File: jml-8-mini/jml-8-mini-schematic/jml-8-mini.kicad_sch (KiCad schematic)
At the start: 7 parts, among them J1 Barrel_Jack, SW1 SW_DPDT_x2, U1 Z80CPU, U2 28HC64, U3 60L256, U4 Z80 CTC, U6 Z80 SIO

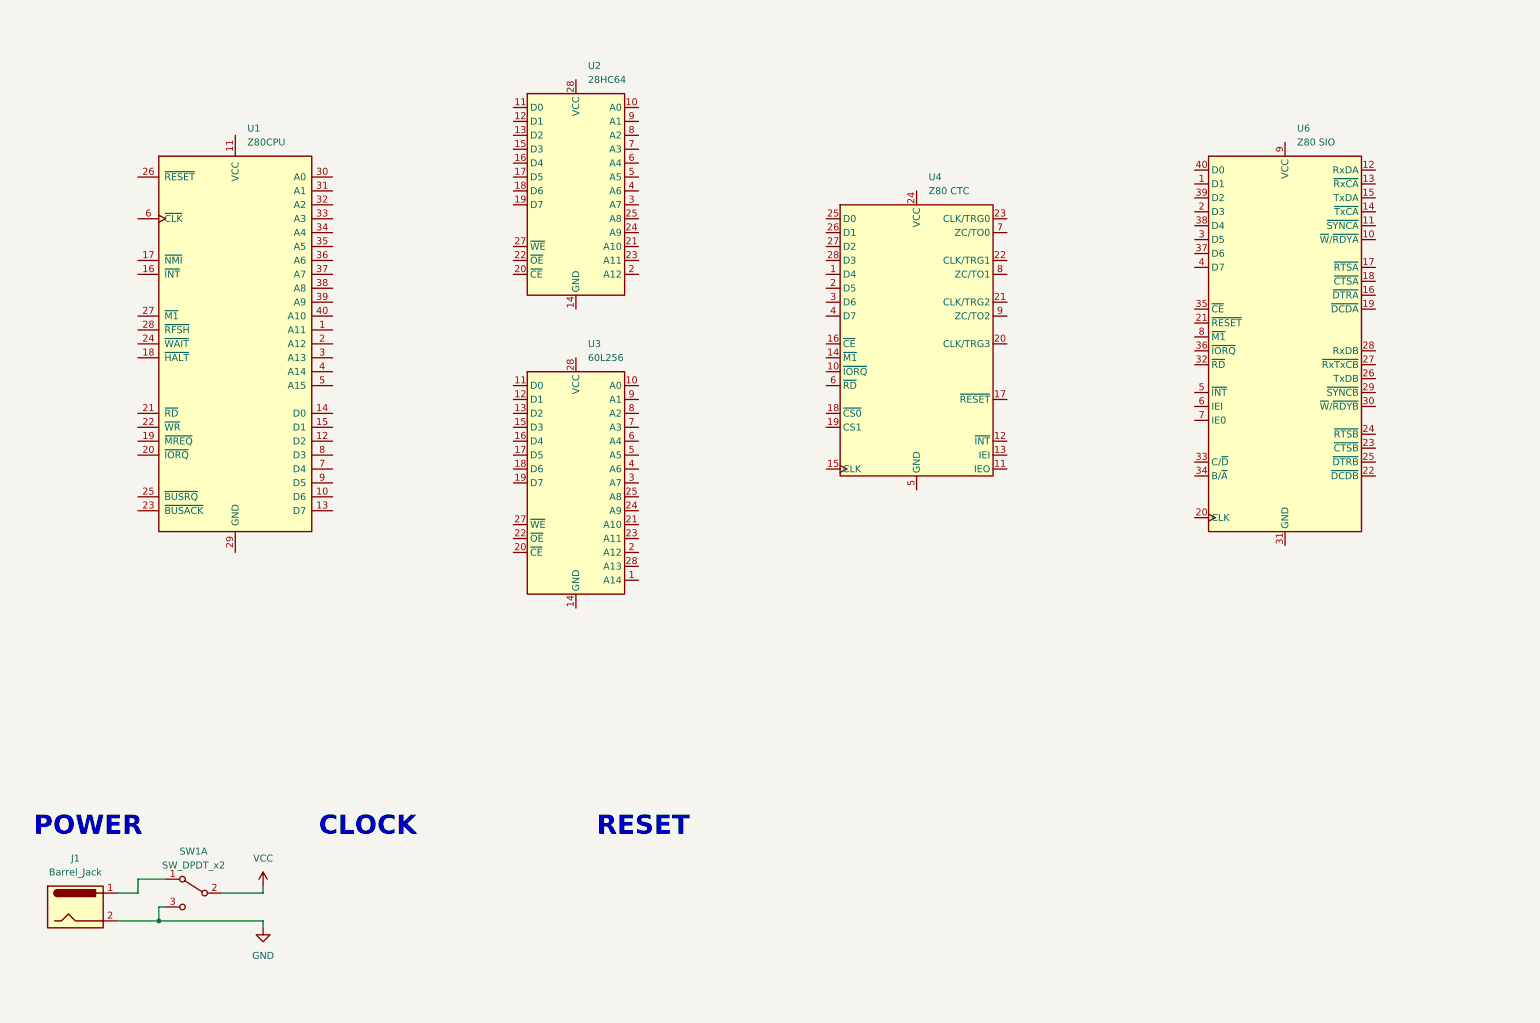
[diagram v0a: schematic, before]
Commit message: updates to jml-8 mini schematic
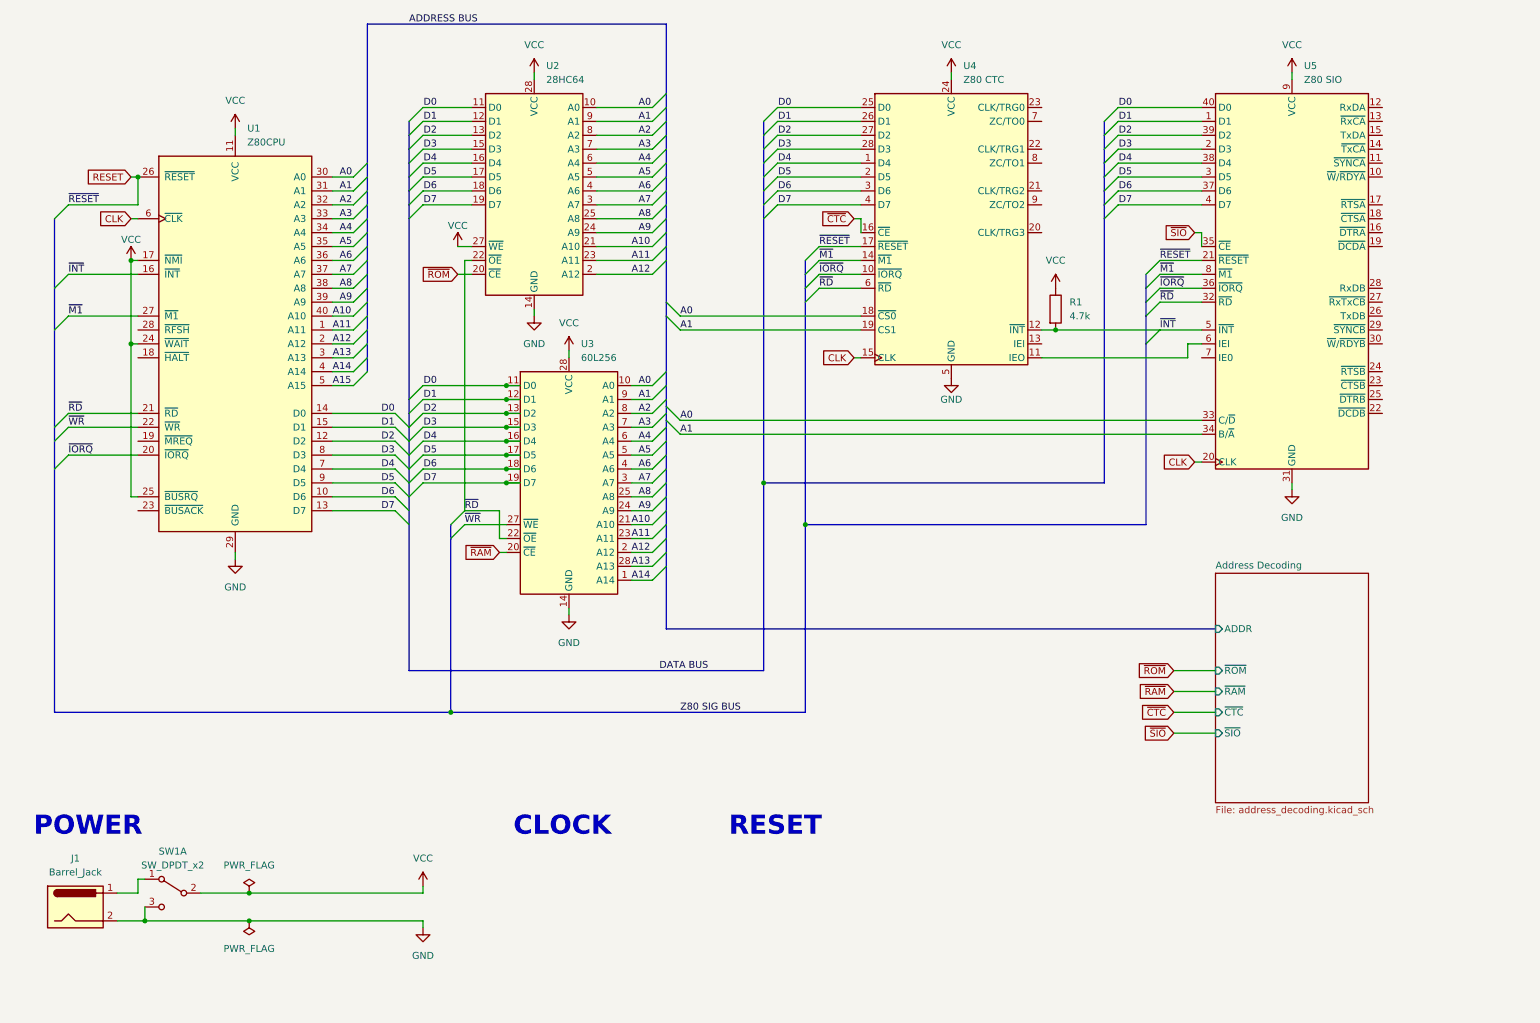
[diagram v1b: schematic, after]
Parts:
- removed U6: Z80 SIO, Package_DIP:DIP-40_W15.24mm_LongPads, symbol jml-8-mini-library:Z80_SIO/0
- added R1: 4.7k, symbol Device:R
- added U5: Z80 SIO, symbol jml-8-mini-library:Z80_SIO/0
- U4: footprint Package_DIP:DIP-28_W15.24mm_LongPads -> (none)
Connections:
- net GND: now also U1.29 (GND), U2.14 (GND), U3.14 (GND), U4.5 (GND), U5.31 (GND)
- net VCC: now also U1.11 (VCC), U1.17 (~{NMI}), U1.24 (~{WAIT}), U1.25 (~{BUSRQ}), U2.27 (~{WE}), U2.28 (VCC), U3.28 (VCC), U4.24 (VCC), R1.1, U5.9 (VCC)
- net A0: now reaches U2.10 (A0)
- net A0: now also U1.30 (A0), U3.10 (A0), U4.18 (~{CS0}), U5.33 (C/~{D})
- net D0: now reaches U2.11 (D0)
- net D0: now also U1.14 (D0), U3.11 (D0), U4.25 (D0), U5.40 (D0)
- net D1: now reaches U2.12 (D1)
- net D1: now also U1.15 (D1), U3.12 (D1), U4.26 (D1), U5.1 (D1)
- net D2: now reaches U2.13 (D2)
- net D2: now also U1.12 (D2), U3.13 (D2), U4.27 (D2), U5.39 (D2)
- net D3: now reaches U2.15 (D3)
- net D3: now also U1.8 (D3), U3.15 (D3), U4.28 (D3), U5.2 (D3)
- net D4: now reaches U2.16 (D4)
- net D4: now also U1.7 (D4), U3.16 (D4), U4.1 (D4), U5.38 (D4)
- net D5: now reaches U2.17 (D5)
- net D5: now also U1.9 (D5), U3.17 (D5), U4.2 (D5), U5.3 (D5)
- net D6: now reaches U2.18 (D6)
- net D6: now also U1.10 (D6), U3.18 (D6), U4.3 (D6), U5.37 (D6)
- net D7: now reaches U2.19 (D7)
- net D7: now also U1.13 (D7), U3.19 (D7), U4.4 (D7), U5.4 (D7)
- net A12: now reaches U2.2 (A12)
- net A12: now also U1.2 (A12), U3.2 (A12)
- net ~{ROM}: now reaches U2.20 (~{CE})
- net A10: now reaches U2.21 (A10)
- net A10: now also U1.40 (A10), U3.21 (A10)
- net ~{RD}: now reaches U2.22 (~{OE})
- net ~{RD}: now also U1.21 (~{RD}), U3.22 (~{OE}), U4.6 (~{RD}), U5.32 (~{RD})
- net A11: now reaches U2.23 (A11)
- net A11: now also U1.1 (A11), U3.23 (A11)
- net A9: now reaches U2.24 (A9)
- net A9: now also U1.39 (A9), U3.24 (A9)
- net A8: now reaches U2.25 (A8)
- net A8: now also U1.38 (A8), U3.25 (A8)
- net A7: now reaches U2.3 (A7)
- net A7: now also U1.37 (A7), U3.3 (A7)
- net A6: now reaches U2.4 (A6)
- net A6: now also U1.36 (A6), U3.4 (A6)
- net A5: now reaches U2.5 (A5)
- net A5: now also U1.35 (A5), U3.5 (A5)
- net A4: now reaches U2.6 (A4)
- net A4: now also U1.34 (A4), U3.6 (A4)
- net A3: now reaches U2.7 (A3)
- net A3: now also U1.33 (A3), U3.7 (A3)
- net A2: now reaches U2.8 (A2)
- net A2: now also U1.32 (A2), U3.8 (A2)
- net A1: now reaches U2.9 (A1)
- net A1: now also U1.31 (A1), U3.9 (A1), U4.19 (CS1), U5.34 (B/~{A})
- net A14: now reaches U3.1 (A14)
- net A14: now also U1.4 (A14)
- net ~{RAM}: now reaches U3.20 (~{CE})
- net ~{WR}: now reaches U3.27 (~{WE})
- net ~{WR}: now also U1.22 (~{WR})
- net ~{IORQ}: now reaches U4.10 (~{IORQ})
- net ~{IORQ}: now also U1.20 (~{IORQ}), U5.36 (~{IORQ})
- net at U4.11 (IEO): now also U5.6 (IEI)
- net ~{INT}: now reaches U4.12 (~{INT})
- net ~{INT}: now also U1.16 (~{INT}), R1.2, U5.5 (~{INT})
- net ~{M1}: now reaches U4.14 (~{M1})
- net ~{M1}: now also U1.27 (~{M1}), U5.8 (~{M1})
- net CLK: now reaches U4.15 (CLK)
- net CLK: now also U1.6 (~{CLK}), U5.20 (CLK)
- net ~{CTC}: now reaches U4.16 (~{CE})
- net RESET: now reaches U4.17 (~{RESET})
- net RESET: now also U1.26 (~{RESET}), U5.21 (~{RESET})
- net A13: now reaches U1.3 (A13)
- net A13: now also U3.28 (VCC)
- net A15: now reaches U1.5 (A15)
- new net ~{SIO}: U5.35 (~{CE})
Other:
- added sheet Address Decoding (address_decoding.kicad_sch)
- moved on the sheet: SW1A, U2, U3

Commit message: update schematic, new program to test RAM
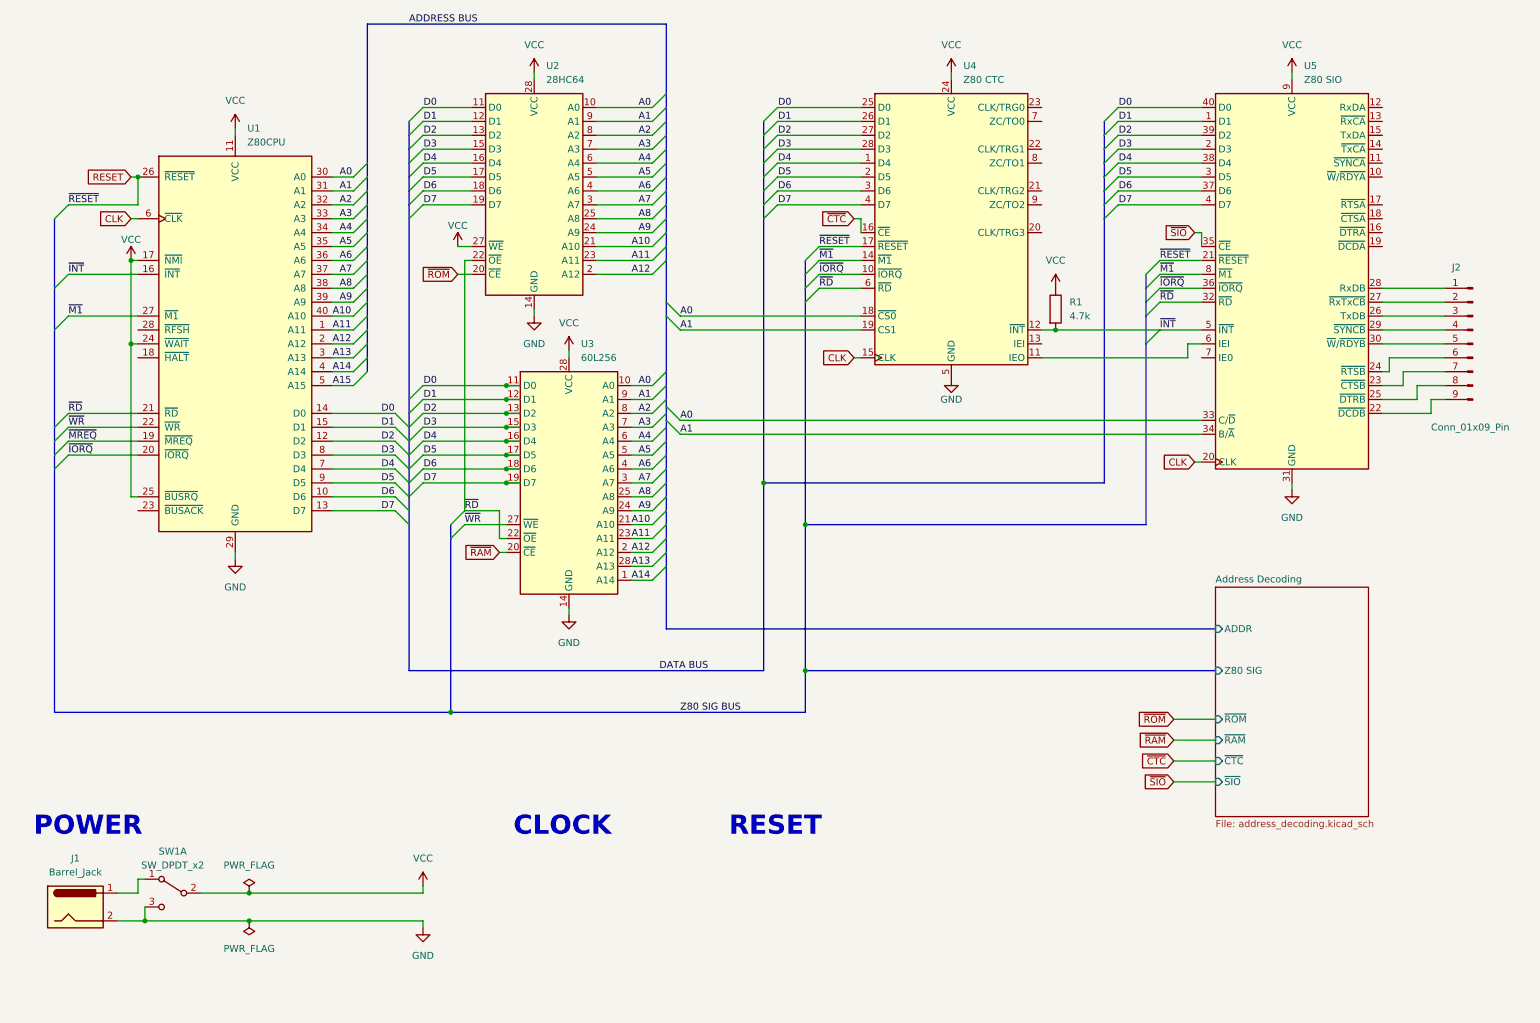
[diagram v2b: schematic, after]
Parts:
- added J2: Conn_01x09_Pin, symbol Connector:Conn_01x09_Pin
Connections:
- net ~{MREQ}: now reaches U1.19 (~{MREQ})
- net at U5.22 (~{DCDB}): now also J2.9 (Pin_9)
- net at U5.23 (~{CTSB}): now also J2.7 (Pin_7)
- net at U5.24 (~{RTSB}): now also J2.6 (Pin_6)
- net at U5.25 (~{DTRB}): now also J2.8 (Pin_8)
- net at U5.26 (TxDB): now also J2.3 (Pin_3)
- net at U5.27 (~{RxTxCB}): now also J2.2 (Pin_2)
- net at U5.28 (RxDB): now also J2.1 (Pin_1)
- net at U5.29 (~{SYNCB}): now also J2.4 (Pin_4)
- net at U5.30 (~{W}/~{RDYB}): now also J2.5 (Pin_5)
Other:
- sheet Address Decoding ports: added Z80 SIG; removed none
